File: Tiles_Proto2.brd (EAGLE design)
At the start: 100 x 80 mm, 47 parts, among them J1 7p-SMD-2.54, U1 ADXL345BCCZ-RL, U2 MPR121QR2, U3 MCP73832T-2ACI/OT-SOT23-5

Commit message: version before starting routing
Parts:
- removed CAP7, CAP8, CAP9: (no value), wirepad:SMD1,27-2,54
- removed USB1: 10118193-0001LF, Seeed-OPL-Connector:MICRO-USB5+6P-SMD-0.65-B
- added CP7, CP8, CP9: (no value), wirepad:SMD1,27-2,54
- added RFDUINO: RF22301, GeekAmmo:RFD22301
- U$1: value RF22301 -> ST-USB-001L5; device GeekAmmo:RFD22301 -> Seeed-OPL-Connector:MICRO-USB5+2P-0.65-180D
- moved JP1 54.6 mm to (23.5, 80.0), turned to 0 degrees
- moved SJ3 45.8 mm to (23.5, 77.5)
- moved SJ4 45.8 mm to (26.0, 77.5)
- moved SJ5 45.8 mm to (28.6, 77.5)
- moved SJ6 45.8 mm to (31.1, 77.5)
- moved SW1 27.9 mm to (4.99, 52.1), turned to 0 degrees
- moved B- 25.6 mm to (27.3, 52.7), turned to 270 degrees
- moved C5 23.8 mm to (24.1, 56.5), turned to 0 degrees
- moved J1 22.4 mm to (12.1, 78.6), turned to 90 degrees
- moved B+ 21.6 mm to (24.1, 52.7), turned to 270 degrees
- moved CAPL 21.1 mm to (64.8, 80.6), flipped to the bottom
- moved R9 19.6 mm to (17.1, 52.7), turned to 90 degrees
- moved CAPR 18.3 mm to (75.6, 76.2), flipped to the bottom
- moved U$1 18.2 mm to (5.00, 40.2)
- moved D3 18.2 mm to (21.0, 53.3), turned to 90 degrees
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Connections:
- net FACTORY: now also RFDUINO.15; no longer U$1.15
- net GND: now also R1.2, R2.2, R3.2, RFDUINO.1, RFDUINO.10, RFDUINO.12, RFDUINO.18, RFDUINO.19, RFDUINO.2, RFDUINO.8, RFDUINO.9, U$1.5; no longer D1.4, D1.5, D1.6, U$1.1, U$1.10, U$1.12, U$1.18, U$1.19, U$1.2, U$1.8, U$1.9, USB1.5
- net HAPTIC: now also RFDUINO.4; no longer U$1.4
- net INT: now also RFDUINO.5; no longer U$1.5
- net LED_B: now also D1.3, RFDUINO.3; no longer R3.1, U$1.3
- net LED_G: now also D1.2, RFDUINO.17; no longer R1.1, U$1.17
- net LED_R: now also D1.1, RFDUINO.16; no longer R2.1, U$1.16
- net N$1: now also D1.5, R1.1; no longer D1.2, R1.2
- net N$2: now also D1.6, R2.1; no longer D1.1, R2.2
- net N$20: now also CP7.1; no longer CAP7.1
- net N$21: now also CP8.1; no longer CAP8.1
- net N$22: now also CP9.1; no longer CAP9.1
- net N$3: now also D1.4, R3.1; no longer D1.3, R3.2
- net N$8: now also U$1.1; no longer USB1.1
- net RESET: now also RFDUINO.14; no longer U$1.14
- net SCL: now also RFDUINO.6; no longer U$1.6
- net SDA: now also RFDUINO.7; no longer U$1.7
- net VCC: now also RFDUINO.13; no longer U$1.13
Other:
- board size 100 x 80 mm -> 50 x 50 mm

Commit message: routing in progress
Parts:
- removed U$1: ST-USB-001L5, Seeed-OPL-Connector:MICRO-USB5+2P-0.65-180D
- removed U$4: MMBT3904LT1G, Seeed-OPL-Transistor:SOT-23
- added Q1: MMBT3904LT1G, Seeed-OPL-Transistor:SOT-23
- added USB1: 10118193-0001LF, Seeed-OPL-Connector:MICRO-USB5+6P-SMD-0.65-B
- moved R1 3.86 mm to (31.1, 63.5)
- moved C3 3.81 mm to (35.6, 71.8), turned to 0 degrees
- moved R11 3.24 mm to (32.4, 73.7)
- moved D2 3.17 mm to (8.26, 57.8)
- moved D1 2.84 mm to (25.4, 62.2)
- moved C1 2.73 mm to (22.2, 67.4), turned to 270 degrees
- moved U1 2.62 mm to (26.0, 70.5)
- moved C6 2.62 mm to (26.0, 56.5)
- moved R2 2.62 mm to (31.1, 66.7)
- moved SJ1 2.01 mm to (34.3, 76.8)
- moved R8 1.80 mm to (21.6, 57.8)
- moved U3 1.64 mm to (12.4, 54.0), turned to 270 degrees
- moved R12 1.42 mm to (30.5, 70.5)
- moved R10 1.42 mm to (19.1, 56.5)
- moved C4 1.27 mm to (15.9, 57.8)
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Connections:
- net GND: now also Q1.2, USB1.5; no longer U$1.5, U$4.2
- net HAPTIC: now also Q1.1; no longer U$4.1
- net N$7: now also Q1.3; no longer U$4.3
- net N$8: now also USB1.1; no longer U$1.1
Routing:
- net GND: track 0.00 -> 173.6 mm, vias 0 -> 10
- net VCC: track 0.00 -> 110.6 mm, vias 0 -> 9
- net SDA: track 0.00 -> 79.8 mm, vias 0 -> 2
- net SCL: track 0.00 -> 50.6 mm, vias 0 -> 6
- net INT: track 0.00 -> 47.7 mm, vias 0 -> 4
- net N$8: track 0.00 -> 35.9 mm, vias 0 -> 4
- net HAPTIC: track 0.00 -> 34.8 mm, vias 0 -> 2
- net LED_G: track 0.00 -> 34.4 mm, vias 0 -> 2
- net VDDI/O: track 0.00 -> 28.0 mm, vias 0 -> 2
- net V_BATT: track 0.00 -> 27.7 mm
- net LED_B: track 0.00 -> 27.2 mm, vias 0 -> 2
- net LED_R: track 0.00 -> 26.8 mm, vias 0 -> 2
- net N$24: track 0.00 -> 26.1 mm, vias 0 -> 2
- net FACTORY: track 0.00 -> 17.6 mm
- net RESET: track 0.00 -> 15.8 mm
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
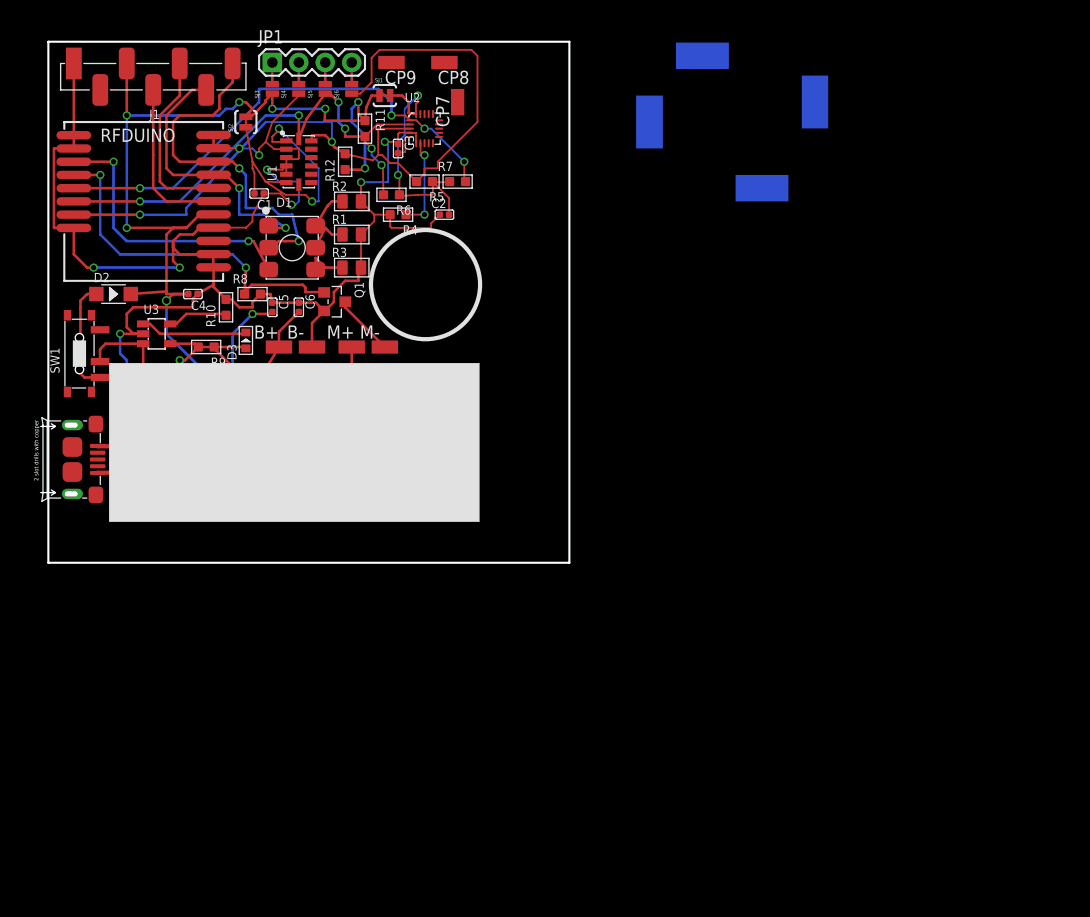
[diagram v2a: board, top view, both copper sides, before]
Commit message: finished routing, no silk screen
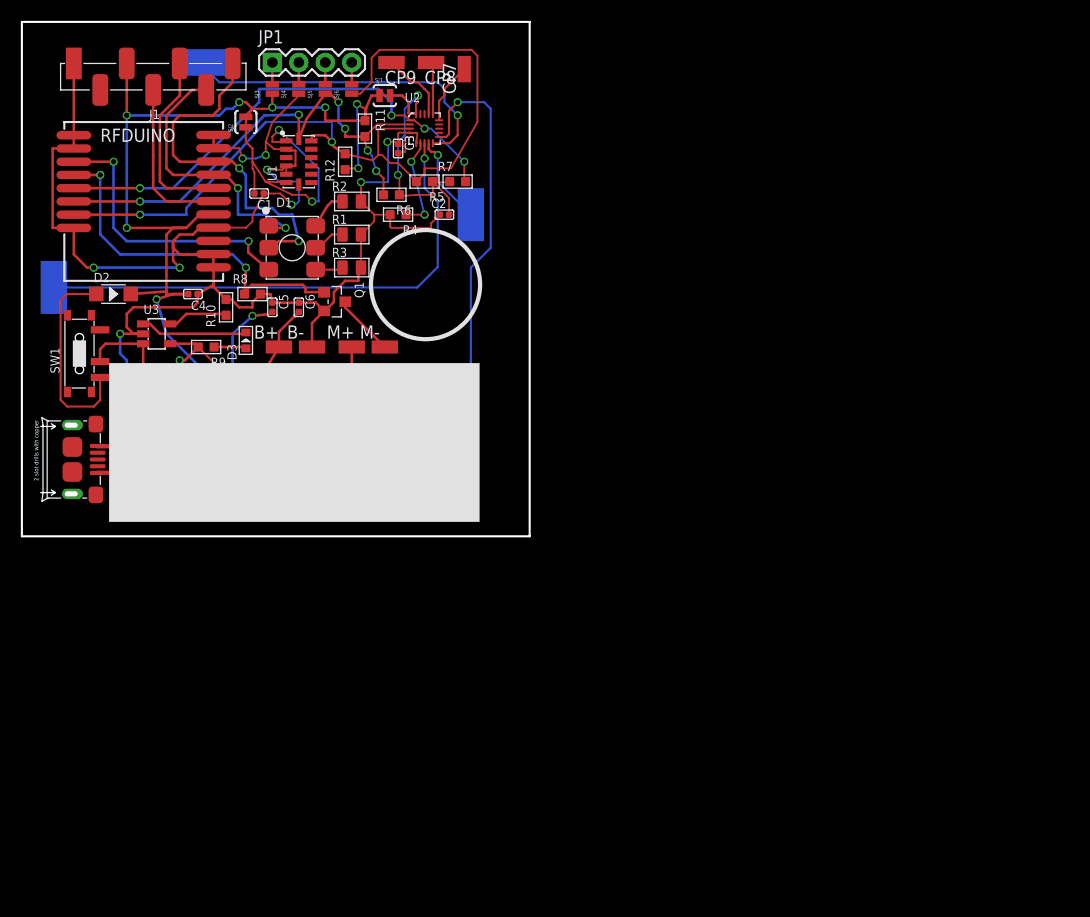
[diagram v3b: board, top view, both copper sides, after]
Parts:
- moved CAPL 66.1 mm to (2.54, 58.4), turned to 0 degrees
- moved CAPT 55.3 mm to (16.5, 80.0)
- moved CAPB 44.4 mm to (34.9, 37.5), turned to 270 degrees
- moved CAPR 34.7 mm to (42.5, 65.4)
- moved CP7 3.24 mm to (41.9, 79.4)
- moved CP8 1.27 mm to (38.7, 80.0)
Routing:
- net N$16: track 0.00 -> 50.0 mm, vias 0 -> 1
- net N$19: track 0.00 -> 49.9 mm, vias 0 -> 1
- net N$18: track 0.00 -> 32.2 mm, vias 0 -> 1
- net N$9: track 10.8 -> 19.7 mm
- net N$17: track 0.00 -> 8.73 mm, vias 0 -> 1
- net N$22: track 0.00 -> 6.80 mm
- net N$20: track 0.00 -> 5.91 mm
- net N$21: track 0.00 -> 5.02 mm
- net VCC: track 110.6 -> 108.4 mm
- net N$3: track 4.08 -> 2.66 mm
- net N$1: track 4.03 -> 3.10 mm
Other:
- board size 50 x 50 mm -> 48.7 x 49.4 mm

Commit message: top silskreen
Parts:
- moved USB1 1.97 mm to (6.99, 39.9)
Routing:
- net GND: track 173.7 -> 174.5 mm
- net N$8: track 35.8 -> 36.6 mm
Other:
- board size 48.7 x 49.4 mm -> 46.2 x 48.1 mm
- board text added: "BATTERY"
- board text added: "CHG"
- board text added: "MOTOR"

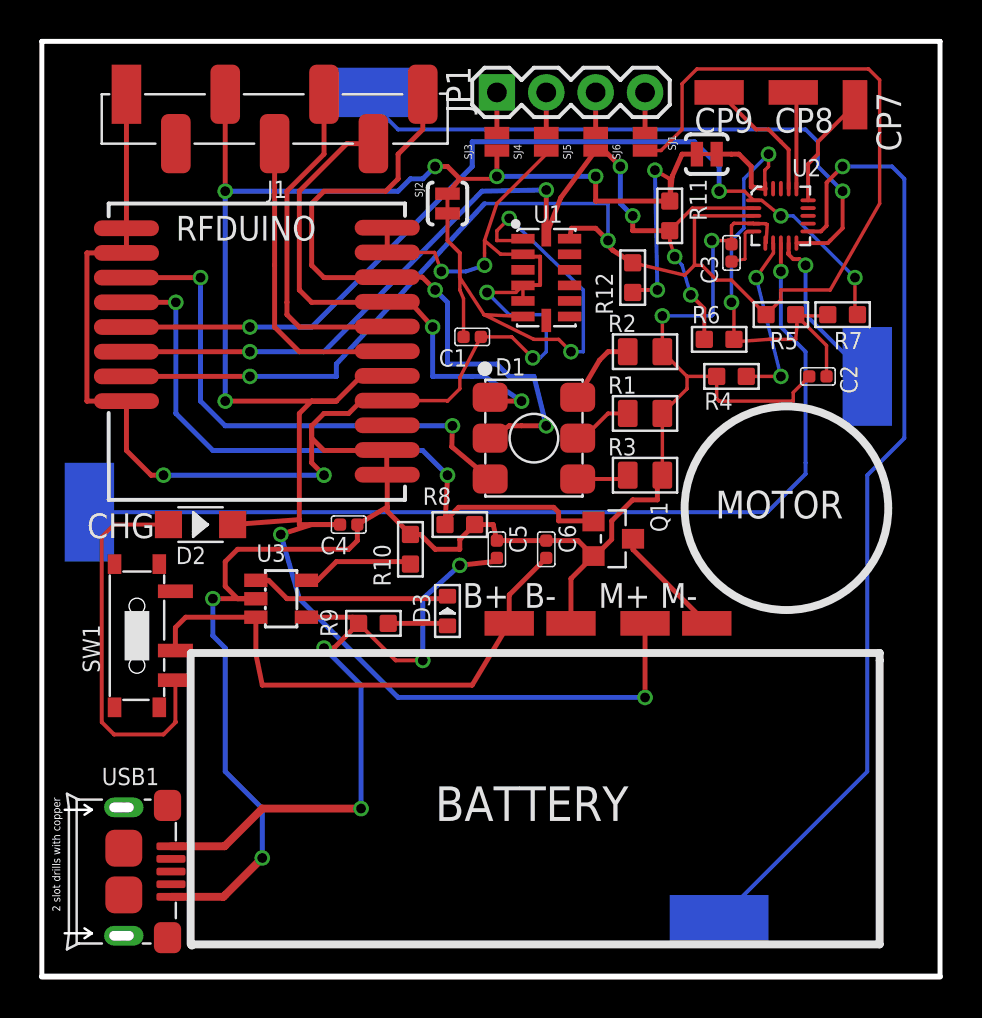
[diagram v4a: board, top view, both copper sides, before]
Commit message: finished silkscreen, no copper pour
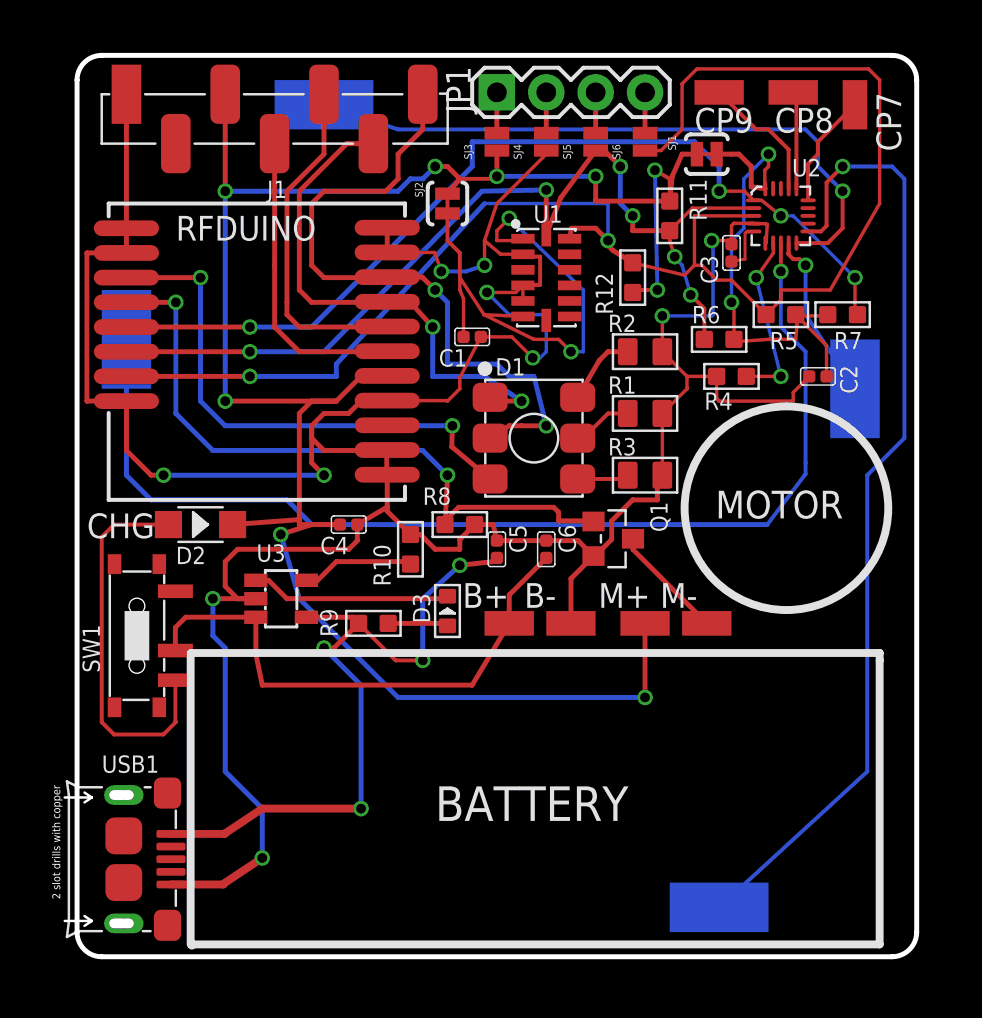
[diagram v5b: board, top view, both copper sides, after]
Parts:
- removed CAPB, CAPL, CAPR, CAPT: (no value), wirepad:SMD2,54-5,08
- added BOTTOM, LEFT, RIGHT, TOP: (no value), wirepad:SMD2,54-5,08
- moved USB1 0.64 mm to (6.99, 40.6)
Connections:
- net N$16: now also LEFT.1; no longer CAPL.1
- net N$17: now also RIGHT.1; no longer CAPR.1
- net N$18: now also TOP.1; no longer CAPT.1
- net N$19: now also BOTTOM.1; no longer CAPB.1
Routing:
- net N$16: track 50.0 -> 56.7 mm
- net N$18: track 32.2 -> 33.5 mm
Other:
- board size 46.2 x 48.1 mm -> 43.2 x 46.4 mm
- board text added: "CAPACITIVE PORTS"
- board text added: "HACKER PORT"
- board text added: "IDI-NTNU"
- board text added: "Prototype #2 RevA (2015)"
- board text added: "TILES"
- board text added: "TOOLKIT"
- board text added: "simone.mora@ntnu.no"
